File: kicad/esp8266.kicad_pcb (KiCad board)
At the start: 2 copper layers, 85 x 75 mm, 62 parts, among them J1 BATT, J10 Green, J11 Blue, J12 White, J13 IO_RGBW, J14 +12V, J15 hole, J16 hole, J17 hole, J18 hole, J2 5 / 12V, J3 CONN FT232RL, J4 RJ12-I2C, J5 RJ12-I2C, J6 Onewire, J7 Onewire, J8 Red, J9 Pad, Q1 BSP75, Q2 BSP75, Q3 BSP75, Q4 BSP75, SW1 RESET, SW2 PROG, U1 ESP-12E, U2 MCP73831-2, U3 MCP1703-33, U4 MS5637, U5 MCP1703-50, U6 Si7020-A20, U7 DS18B20

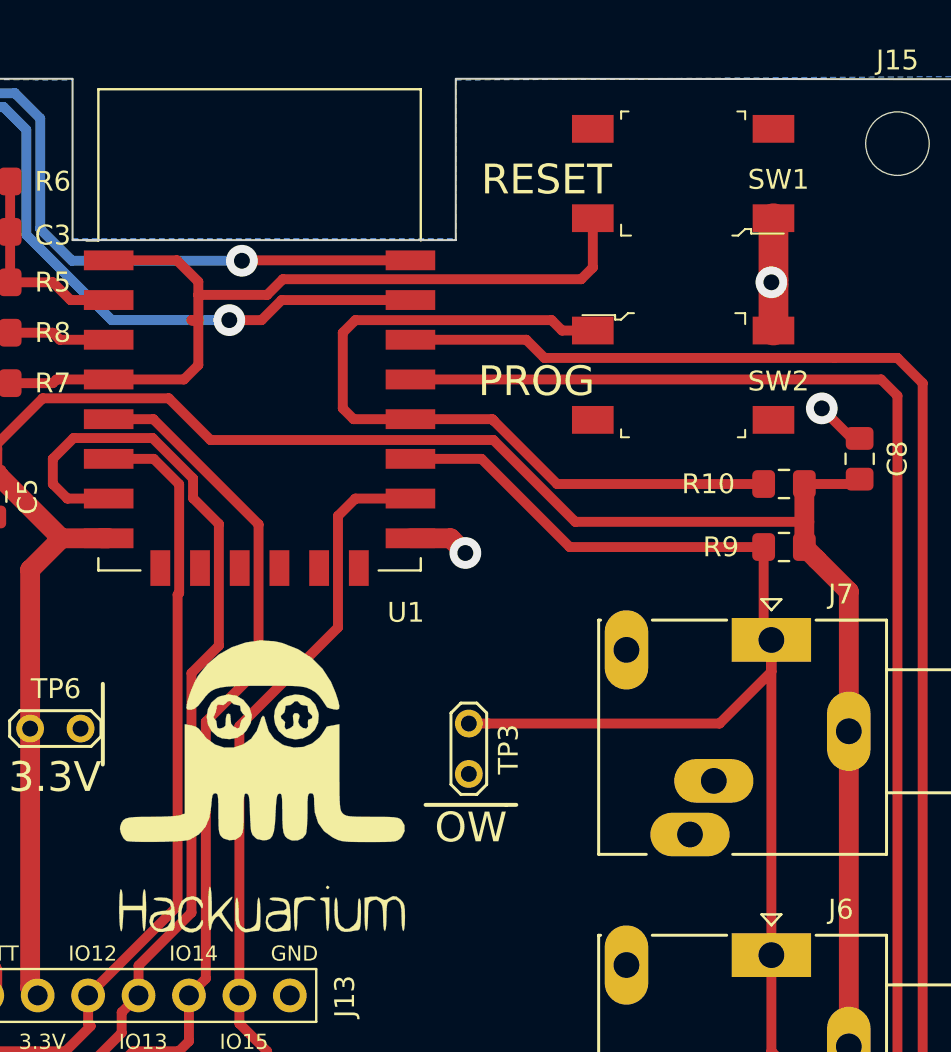
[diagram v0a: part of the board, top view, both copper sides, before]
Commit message: fix resistor on IO15 and button
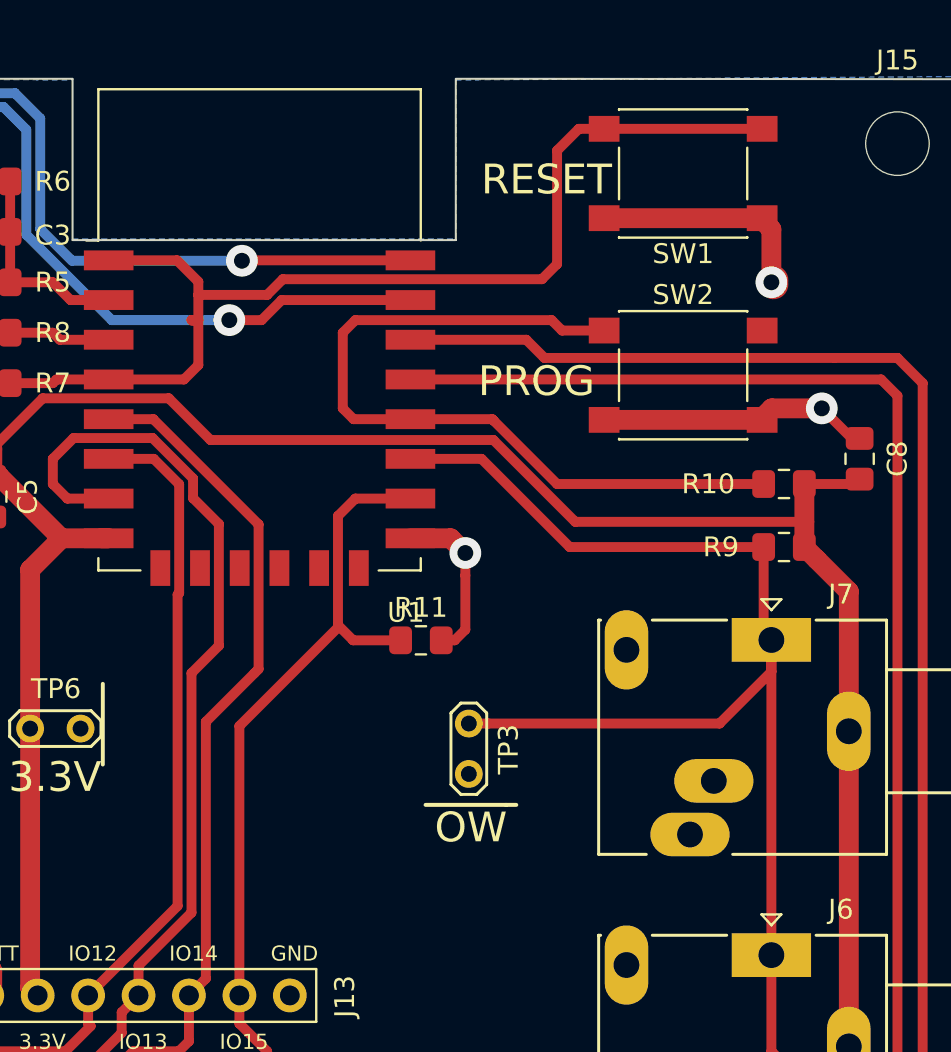
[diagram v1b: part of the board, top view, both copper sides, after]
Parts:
- removed G***: LOGO, hackuarium:hackuarium
- added R11: 10k, Resistor_SMD:R_0805_2012Metric_Pad1.15x1.40mm_HandSolder, F.Cu at (135.9, 90.3)
- SW1, SW2: footprint digikey-footprints:Switch_Tactile_SMD_6x6mm -> Button_Switch_SMD:SW_SPST_PTS645
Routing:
- net GND: track 93.4 -> 115.8 mm
- net /RST: track 42.3 -> 54.8 mm
- net /IO15: track 43.3 -> 46.8 mm
